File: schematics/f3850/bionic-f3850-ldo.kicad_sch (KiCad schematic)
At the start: 11 parts, among them J1 Bionic-P135, J2 Bionic-P245, U1 F3850, U2 11AA010-I/TT, U3 LM78L12

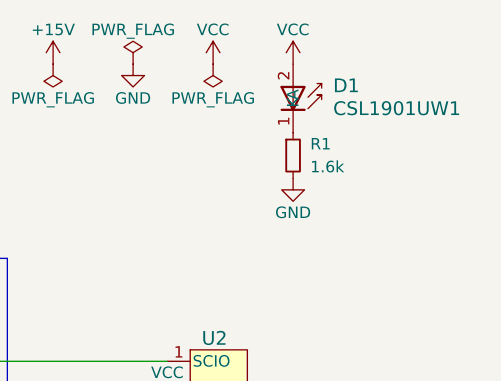
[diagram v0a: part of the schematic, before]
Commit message: [F3850] Rename LDO version
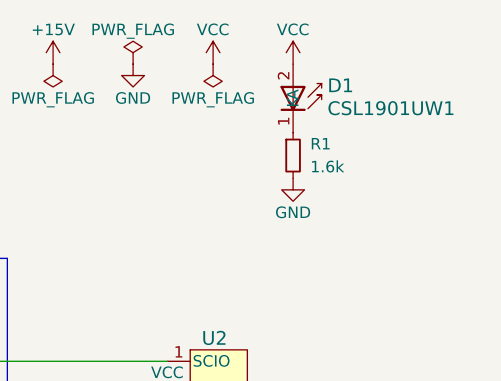
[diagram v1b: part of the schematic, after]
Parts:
- D1: footprint 0-LocalLibrary:LED_CSL1901UW1_ROM-M -> rhom:LED_CSL1901UW1_ROM-M; symbol 0-LocalLibrary:CSL1901UW1 -> rhom:CSL1901UW1
- J1: footprint 0-LocalLibrary:Bionic-P135_Vertical -> connector:Bionic-P135_Vertical; symbol 0-LocalLibrary:Bionic-P135 -> bionic:Bionic-P135
- J2: footprint 0-LocalLibrary:Bionic-P245_Vertical -> connector:Bionic-P245_Vertical; symbol 0-LocalLibrary:Bionic-P245 -> bionic:Bionic-P245
- U1: footprint 0-LocalLibrary:DIP-40_W15.24mm_Socket -> bionic:DIP-40_W15.24mm_Socket; symbol 0-LocalLibrary:F3850 -> cpu:F3850
- U2: footprint 0-LocalLibrary:SOT-23_MC_MCH-M -> microchip:SOT-23_MC_MCH-M; symbol 0-LocalLibrary:11AA010-I_TT -> microchip:11AA010-I_TT
- U3: footprint 0-LocalLibrary:SOT-89-3_Handsoldering -> Package_TO_SOT_SMD:SOT-89-3_Handsoldering
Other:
- title: BionicF3850 -> BionicF3850 LDO
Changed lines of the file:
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@@
 	(paper "A4")
 	(title_block
-		(title "BionicF3850")
+		(title "BionicF3850 LDO")
 		(date "2024-12-11")
 		(rev "6")
@@
 	)
 	(symbol
-		(lib_id "0-LocalLibrary:F3850")
+		(lib_id "cpu:F3850")
 		(at 91.44 93.98 0)
 		(unit 1)
@@
 			)
 		)
-		(property "Footprint" "0-LocalLibrary:DIP-40_W15.24mm_Socket"
+		(property "Footprint" "bionic:DIP-40_W15.24mm_Socket"
 			(at 90.17 128.27 0)
 			(effects
@@
 			)
 		)
-		(property "Description" ""
+		(property "Description" "8-bit Central Processing Unit, DIP-40"
 			(at 91.44 93.98 0)
 			(effects
@@
 	)
 	(symbol
-		(lib_id "0-LocalLibrary:Bionic-P135")
+		(lib_id "bionic:Bionic-P135")
 		(at 156.21 91.44 0)
 		(unit 1)
@@
 			)
 		)
-		(property "Footprint" "0-LocalLibrary:Bionic-P135_Vertical"
+		(property "Footprint" "connector:Bionic-P135_Vertical"
 			(at 157.48 127 0)
 			(effects
@@
 			)
 		)
-		(property "Description" ""
+		(property "Description" "Generic connector, single row, 01x24, script generated (kicad-library-utils/schlib/autogen/connector/)"
 			(at 156.21 91.44 0)
 			(effects
@@
 	)
 	(symbol
-		(lib_id "0-LocalLibrary:CSL1901UW1")
+		(lib_id "rhom:CSL1901UW1")
 		(at 210.82 33.02 270)
 		(unit 1)
@@
 		(fields_autoplaced yes)
 		(property "Reference" "D1"
-			(at 215.265 35.433 90)
+			(at 214.63 35.4329 90)
 			(effects
 				(font
@@
 		)
 		(property "Value" "CSL1901UW1"
-			(at 215.265 37.973 90)
+			(at 214.63 37.9729 90)
 			(effects
 				(font
@@
 			)
 		)
-		(property "Footprint" "0-LocalLibrary:LED_CSL1901UW1_ROM-M"
+		(property "Footprint" "rhom:LED_CSL1901UW1_ROM-M"
 			(at 201.93 36.83 0)
 			(effects
@@
 			)
 		)
-		(property "Description" ""
+		(property "Description" "Red LED (Low Current Emission, SMD)"
 			(at 210.82 33.02 0)
 			(effects
@@
 	)
 	(symbol
-		(lib_id "0-LocalLibrary:Bionic-P245")
+		(lib_id "bionic:Bionic-P245")
 		(at 163.83 91.44 0)
 		(unit 1)
@@
 			)
 		)
-		(property "Footprint" "0-LocalLibrary:Bionic-P245_Vertical"
+		(property "Footprint" "connector:Bionic-P245_Vertical"
 			(at 165.1 127 0)
 			(effects
@@
 			)
 		)
-		(property "Description" ""
+		(property "Description" "Generic connector, single row, 01x24, script generated (kicad-library-utils/schlib/autogen/connector/)"
 			(at 163.83 91.44 0)
 			(effects
@@
 			)
 		)
-		(property "Footprint" "0-LocalLibrary:SOT-89-3_Handsoldering"
+		(property "Footprint" "Package_TO_SOT_SMD:SOT-89-3_Handsoldering"
 			(at 92.71 136.525 0)
 			(effects
@@
 	)
 	(symbol
-		(lib_id "0-LocalLibrary:11AA010-I_TT")
+		(lib_id "microchip:11AA010-I_TT")
 		(at 199.39 64.77 0)
 		(unit 1)
@@
 			)
 		)
-		(property "Footprint" "0-LocalLibrary:SOT-23_MC_MCH-M"
+		(property "Footprint" "microchip:SOT-23_MC_MCH-M"
 			(at 201.93 82.55 0)
 			(effects
@@
 			)
 		)
-		(property "Description" ""
+		(property "Description" "UNI/O Serial EEPROM (1Kbit)"
 			(at 199.39 64.77 0)
 			(effects
